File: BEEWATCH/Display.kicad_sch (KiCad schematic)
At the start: 6 parts, among them Q2 2N7002

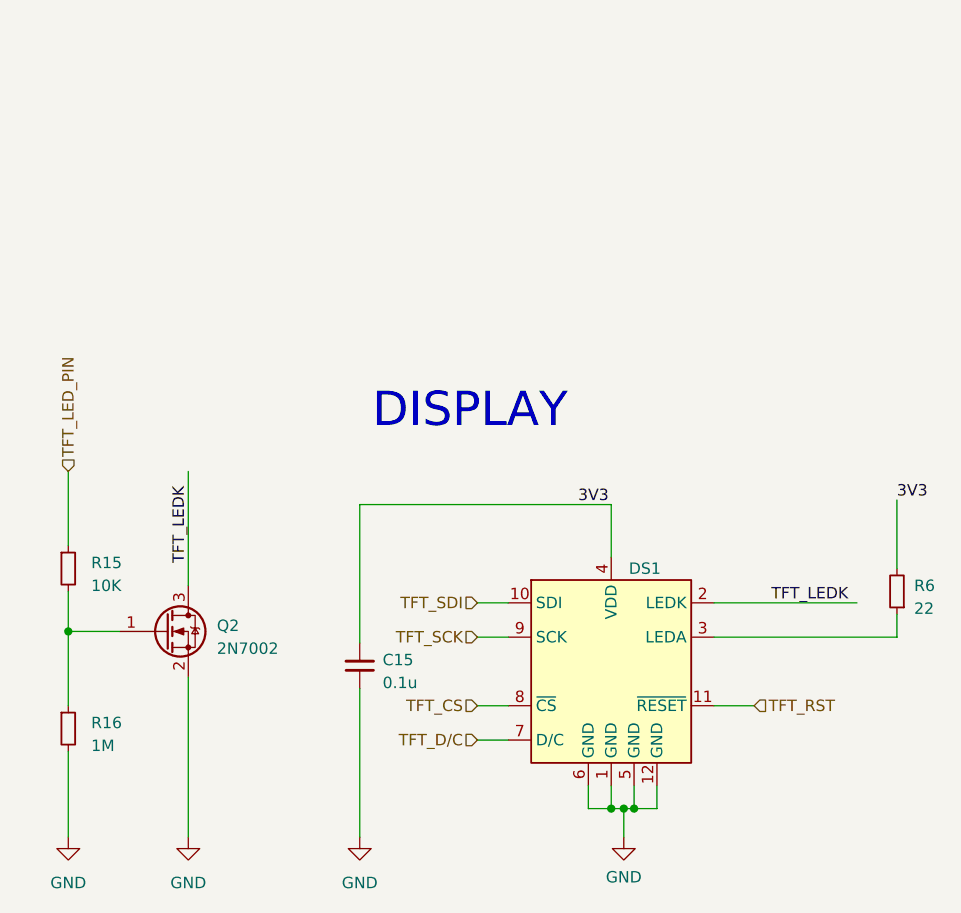
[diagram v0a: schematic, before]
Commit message: Inverted F Antenna designed
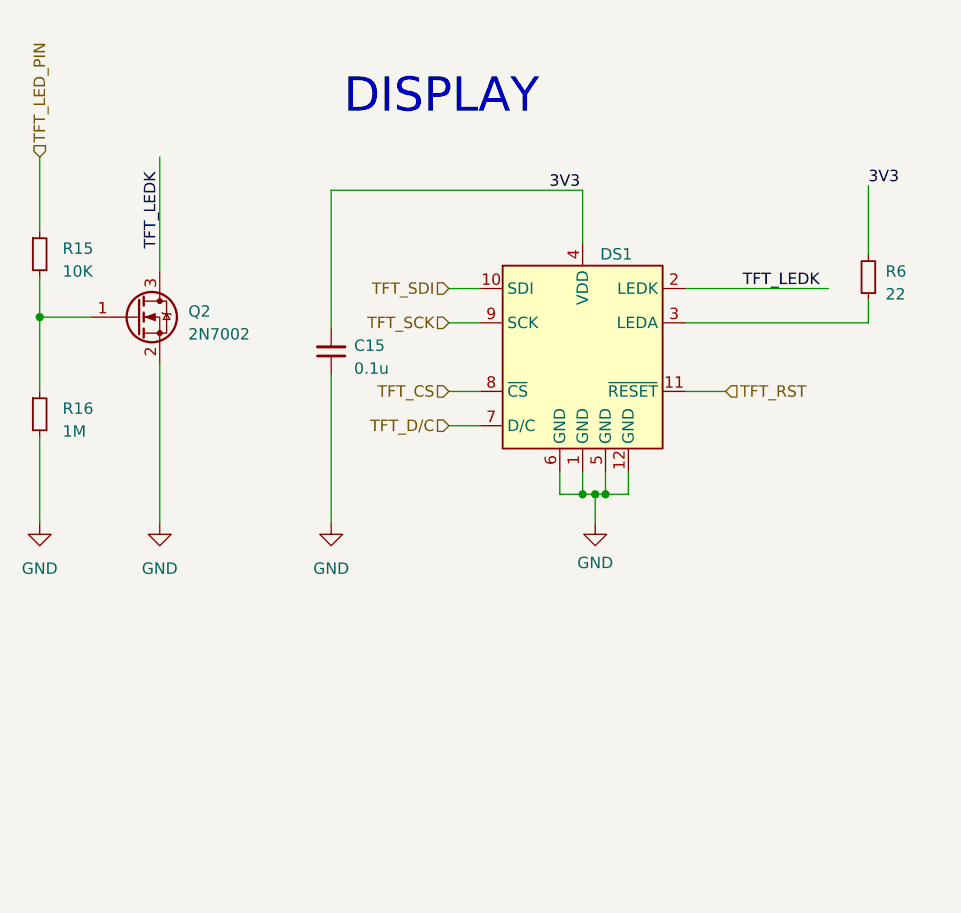
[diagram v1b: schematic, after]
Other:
- moved on the sheet: C15, DS1, Q2, R15, R16, R6

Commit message: Save Kicad files
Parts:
- renumbered C15 to C21, Q2 to Q1, R6 to R16, R16 to R17
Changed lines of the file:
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@@
   (symbol (lib_id "Device:R_Small") (at 190.5 64.135 180) (unit 1)
     (in_bom yes) (on_board yes) (dnp no) (fields_autoplaced)
-    (property "Reference" "R6" (at 192.405 63.5 0)
+    (property "Reference" "R16" (at 192.405 63.5 0)
       (effects (font (size 1.27 1.27)) (justify right))
     )
@@
       (project "BEEWATCH"
         (path "/e9c5fb53-480b-4989-8495-a3341ee99514/15b9618d-10d4-4333-8312-f49228536273"
-          (reference "R6") (unit 1)
+          (reference "R16") (unit 1)
         )
       )
@@
   (symbol (lib_id "power:GND") (at 111.76 91.44 0) (unit 1)
     (in_bom yes) (on_board yes) (dnp no) (fields_autoplaced)
-    (property "Reference" "#PWR020" (at 111.76 97.79 0)
+    (property "Reference" "#PWR018" (at 111.76 97.79 0)
       (effects (font (size 1.27 1.27)) hide)
     )
@@
       (project "BEEWATCH"
         (path "/e9c5fb53-480b-4989-8495-a3341ee99514/15b9618d-10d4-4333-8312-f49228536273"
+          (reference "#PWR018") (unit 1)
+        )
+      )
+    )
+  )
+  (symbol (lib_id "power:GND") (at 160.147 91.44 0) (unit 1)
+    (in_bom yes) (on_board yes) (dnp no) (fields_autoplaced)
+    (property "Reference" "#PWR020" (at 160.147 97.79 0)
+      (effects (font (size 1.27 1.27)) hide)
+    )
+    (property "Value" "GND" (at 160.147 95.885 0)
+      (effects (font (size 1.27 1.27)))
+    )
+    (property "Footprint" "" (at 160.147 91.44 0)
+      (effects (font (size 1.27 1.27)) hide)
+    )
+    (property "Datasheet" "" (at 160.147 91.44 0)
+      (effects (font (size 1.27 1.27)) hide)
+    )
+    (pin "1")
+    (instances
+      (project "BEEWATCH"
+        (path "/e9c5fb53-480b-4989-8495-a3341ee99514/15b9618d-10d4-4333-8312-f49228536273"
           (reference "#PWR020") (unit 1)
         )
@@
     )
   )
-  (symbol (lib_id "power:GND") (at 160.147 91.44 0) (unit 1)
-    (in_bom yes) (on_board yes) (dnp no) (fields_autoplaced)
-    (property "Reference" "#PWR013" (at 160.147 97.79 0)
-      (effects (font (size 1.27 1.27)) hide)
-    )
-    (property "Value" "GND" (at 160.147 95.885 0)
-      (effects (font (size 1.27 1.27)))
-    )
-    (property "Footprint" "" (at 160.147 91.44 0)
-      (effects (font (size 1.27 1.27)) hide)
-    )
-    (property "Datasheet" "" (at 160.147 91.44 0)
-      (effects (font (size 1.27 1.27)) hide)
-    )
-    (pin "1")
-    (instances
-      (project "BEEWATCH"
-        (path "/e9c5fb53-480b-4989-8495-a3341ee99514/15b9618d-10d4-4333-8312-f49228536273"
-          (reference "#PWR013") (unit 1)
-        )
-      )
-    )
-  )
   (symbol (lib_id "Device:C_Small") (at 130.81 72.39 180) (unit 1)
     (in_bom yes) (on_board yes) (dnp no) (fields_autoplaced)
-    (property "Reference" "C15" (at 133.35 71.7486 0)
+    (property "Reference" "C21" (at 133.35 71.7486 0)
       (effects (font (size 1.27 1.27)) (justify right))
     )
@@
       (project "BEEWATCH"
         (path "/e9c5fb53-480b-4989-8495-a3341ee99514/15b9618d-10d4-4333-8312-f49228536273"
-          (reference "C15") (unit 1)
+          (reference "C21") (unit 1)
         )
       )
@@
   (symbol (lib_id "power:GND") (at 98.425 91.44 0) (unit 1)
     (in_bom yes) (on_board yes) (dnp no) (fields_autoplaced)
-    (property "Reference" "#PWR021" (at 98.425 97.79 0)
+    (property "Reference" "#PWR017" (at 98.425 97.79 0)
       (effects (font (size 1.27 1.27)) hide)
     )
@@
       (project "BEEWATCH"
         (path "/e9c5fb53-480b-4989-8495-a3341ee99514/15b9618d-10d4-4333-8312-f49228536273"
-          (reference "#PWR021") (unit 1)
+          (reference "#PWR017") (unit 1)
         )
       )
@@
   (symbol (lib_id "Transistor_FET:2N7002") (at 109.22 68.58 0) (unit 1)
     (in_bom yes) (on_board yes) (dnp no) (fields_autoplaced)
-    (property "Reference" "Q2" (at 114.935 67.945 0)
+    (property "Reference" "Q1" (at 114.935 67.945 0)
       (effects (font (size 1.27 1.27)) (justify left))
     )
@@
       (project "BEEWATCH"
         (path "/e9c5fb53-480b-4989-8495-a3341ee99514/15b9618d-10d4-4333-8312-f49228536273"
-          (reference "Q2") (unit 1)
+          (reference "Q1") (unit 1)
         )
       )
@@
   (symbol (lib_id "power:GND") (at 130.81 91.44 0) (unit 1)
     (in_bom yes) (on_board yes) (dnp no) (fields_autoplaced)
-    (property "Reference" "#PWR014" (at 130.81 97.79 0)
+    (property "Reference" "#PWR019" (at 130.81 97.79 0)
       (effects (font (size 1.27 1.27)) hide)
     )
@@
       (project "BEEWATCH"
         (path "/e9c5fb53-480b-4989-8495-a3341ee99514/15b9618d-10d4-4333-8312-f49228536273"
-          (reference "#PWR014") (unit 1)
+          (reference "#PWR019") (unit 1)
         )
       )
@@
   (symbol (lib_id "Device:R_Small") (at 98.425 79.375 0) (unit 1)
     (in_bom yes) (on_board yes) (dnp no) (fields_autoplaced)
-    (property "Reference" "R16" (at 100.965 78.74 0)
+    (property "Reference" "R17" (at 100.965 78.74 0)
       (effects (font (size 1.27 1.27)) (justify left))
     )
@@
       (project "BEEWATCH"
         (path "/e9c5fb53-480b-4989-8495-a3341ee99514/15b9618d-10d4-4333-8312-f49228536273"
-          (reference "R16") (unit 1)
-        )
-      )
+          (reference "R17") (unit 1)
+        )
+      )
